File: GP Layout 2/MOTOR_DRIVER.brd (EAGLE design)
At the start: 91.4 x 97.5 mm, 52 parts, among them U3 MIC4604YM, U6 MIC4604YM, U7 ATMEGA328P_TQFP, Y1 16MHz

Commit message: checking that its updated
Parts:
- renumbered BOT_REVERSE to BOT_REV, TOP_REVERSE to TOP_REV, U3 to GATE1, U6 to GATE2
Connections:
- net BLT_RX: now also U$1.8; no longer U$1.7
- net BLT_TX: now also U$1.7; no longer U$1.8
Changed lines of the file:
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@@
 <attribute name="VENDOR" value="TEXAS INSTRUMENTS" x="10.668" y="87.63" size="1.778" layer="27" rot="R90" display="off"/>
 </element>
-<element name="BOT_REVERSE" library="CSD18502KCS" package="KCS3" value="CSD18502KCS_KCS_3" x="16.764" y="87.63" rot="R90">
+<element name="BOT_REV" library="CSD18502KCS" package="KCS3" value="CSD18502KCS_KCS_3" x="16.764" y="87.63" rot="R90">
 <attribute name="MANUFACTURER_PART_NUMBER" value="csd18502kcs_kcs_3" x="16.764" y="87.63" size="1.778" layer="27" rot="R90" display="off"/>
 <attribute name="VENDOR" value="TEXAS INSTRUMENTS" x="16.764" y="87.63" size="1.778" layer="27" rot="R90" display="off"/>
 </element>
-<element name="U3" library="MIC4604" package="SOIC-8_M" value="MIC4604YM" x="17.78" y="74.93" rot="MR270">
+<element name="GATE1" library="MIC4604" package="SOIC-8_M" value="MIC4604YM" x="17.78" y="74.93" rot="MR270">
 <attribute name="MANUFACTURER_PART_NUMBER" value="mic4604ym" x="17.78" y="74.93" size="1.778" layer="28" rot="MR270" display="off"/>
 <attribute name="VENDOR" value="Microchip" x="17.78" y="74.93" size="1.778" layer="28" rot="MR270" display="off"/>
 </element>
-<element name="TOP_REVERSE" library="CSD18502KCS" package="KCS3" value="CSD18502KCS_KCS_3" x="16.51" y="60.96" rot="R270">
+<element name="TOP_REV" library="CSD18502KCS" package="KCS3" value="CSD18502KCS_KCS_3" x="16.51" y="60.96" rot="R270">
 <attribute name="MANUFACTURER_PART_NUMBER" value="csd18502kcs_kcs_3" x="16.51" y="60.96" size="1.778" layer="27" rot="R270" display="off"/>
 <attribute name="VENDOR" value="TEXAS INSTRUMENTS" x="16.51" y="60.96" size="1.778" layer="27" rot="R270" display="off"/>
@@
 <attribute name="VENDOR" value="TEXAS INSTRUMENTS" x="10.16" y="60.96" size="1.778" layer="27" rot="R270" display="off"/>
 </element>
-<element name="U6" library="MIC4604" package="SOIC-8_M" value="MIC4604YM" x="30.48" y="74.93" rot="MR270">
+<element name="GATE2" library="MIC4604" package="SOIC-8_M" value="MIC4604YM" x="30.48" y="74.93" rot="MR270">
 <attribute name="MANUFACTURER_PART_NUMBER" value="mic4604ym" x="30.48" y="74.93" size="1.778" layer="28" rot="MR270" display="off"/>
 <attribute name="VENDOR" value="Microchip" x="30.48" y="74.93" size="1.778" layer="28" rot="MR270" display="off"/>
@@
 </signal>
 <signal name="N$2">
-<contactref element="U3" pad="8"/>
-<contactref element="BOT_REVERSE" pad="1"/>
+<contactref element="GATE1" pad="8"/>
+<contactref element="BOT_REV" pad="1"/>
 <wire x1="15.875" y1="72.2757" x2="16.764" y2="82.55" width="0" layer="19" extent="16-16"/>
 </signal>
 <signal name="N$3">
 <contactref element="TOP_FWD" pad="1"/>
-<contactref element="U3" pad="3"/>
+<contactref element="GATE1" pad="3"/>
 <wire x1="10.668" y1="82.55" x2="18.415" y2="77.5843" width="0" layer="19" extent="16-16"/>
 </signal>
 <signal name="N$4">
-<contactref element="U3" pad="4"/>
+<contactref element="GATE1" pad="4"/>
 <contactref element="C2" pad="1"/>
 <contactref element="C1" pad="1"/>
@@
 </signal>
 <signal name="N$5">
-<contactref element="U3" pad="2"/>
+<contactref element="GATE1" pad="2"/>
 <contactref element="C2" pad="2"/>
 <contactref element="C1" pad="2"/>
@@
 </signal>
 <signal name="N$9">
-<contactref element="U6" pad="8"/>
+<contactref element="GATE2" pad="8"/>
 <contactref element="BOT_FWD" pad="1"/>
 <wire x1="10.16" y1="66.04" x2="28.575" y2="72.2757" width="0" layer="19" extent="16-16"/>
 </signal>
 <signal name="N$10">
-<contactref element="TOP_REVERSE" pad="1"/>
-<contactref element="U6" pad="3"/>
+<contactref element="TOP_REV" pad="1"/>
+<contactref element="GATE2" pad="3"/>
 <wire x1="16.51" y1="66.04" x2="31.115" y2="77.5843" width="0" layer="19" extent="16-16"/>
 </signal>
 <signal name="N$11">
-<contactref element="U6" pad="4"/>
+<contactref element="GATE2" pad="4"/>
 <contactref element="C4" pad="1"/>
 <contactref element="C3" pad="1"/>
@@
 </signal>
 <signal name="N$12">
-<contactref element="U6" pad="2"/>
+<contactref element="GATE2" pad="2"/>
 <contactref element="C4" pad="2"/>
 <contactref element="C3" pad="2"/>
@@
 </signal>
 <signal name="BLT_RX">
+<contactref element="BLUETOOTH" pad="1"/>
+<contactref element="U$1" pad="8"/>
+<wire x1="27.624" y1="9.598" x2="52.07" y2="35.666" width="0" layer="19" extent="1-1"/>
+</signal>
+<signal name="BLT_TX">
+<contactref element="BLUETOOTH" pad="2"/>
 <contactref element="U$1" pad="7"/>
-<contactref element="BLUETOOTH" pad="1"/>
-<wire x1="25.084" y1="9.598" x2="52.07" y2="35.666" width="0" layer="19" extent="1-1"/>
-</signal>
-<signal name="BLT_TX">
-<contactref element="U$1" pad="8"/>
-<contactref element="BLUETOOTH" pad="2"/>
-<wire x1="27.624" y1="9.598" x2="54.61" y2="35.666" width="0" layer="19" extent="1-1"/>
+<wire x1="25.084" y1="9.598" x2="54.61" y2="35.666" width="0" layer="19" extent="1-1"/>
 </signal>
 <signal name="N$13">
@@
 <contactref element="D3" pad="A1"/>
 <contactref element="TOP_FWD" pad="2"/>
-<contactref element="U3" pad="1"/>
-<contactref element="TOP_REVERSE" pad="2"/>
-<contactref element="U6" pad="1"/>
+<contactref element="GATE1" pad="1"/>
+<contactref element="TOP_REV" pad="2"/>
+<contactref element="GATE2" pad="1"/>
 <contactref element="BIG_SWITCH" pad="GND"/>
 <wire x1="16.51" y1="63.5" x2="-61.39" y2="82.042" width="0" layer="19" extent="1-1"/>
@@
 <signal name="GND_TOP">
 <contactref element="SV5" pad="10"/>
-<contactref element="BOT_REVERSE" pad="3"/>
-<contactref element="U3" pad="7"/>
+<contactref element="BOT_REV" pad="3"/>
+<contactref element="GATE1" pad="7"/>
 <contactref element="BOT_FWD" pad="3"/>
-<contactref element="U6" pad="7"/>
+<contactref element="GATE2" pad="7"/>
 <contactref element="C12" pad="-"/>
 <contactref element="C15" pad="-"/>
@@
 <signal name="MOTOR_HIGH_TOP">
 <contactref element="TOP_FWD" pad="3"/>
-<contactref element="BOT_REVERSE" pad="2"/>
+<contactref element="BOT_REV" pad="2"/>
 <contactref element="LSP3" pad="MP"/>
 <contactref element="SV6" pad="5"/>
@@
 </signal>
 <signal name="MOTOR_LOW_TOP">
-<contactref element="TOP_REVERSE" pad="3"/>
+<contactref element="TOP_REV" pad="3"/>
 <contactref element="BOT_FWD" pad="2"/>
 <contactref element="LSP6" pad="MP"/>
@@
 <signal name="LI1_TOP">
 <contactref element="SV6" pad="2"/>
-<contactref element="U3" pad="6"/>
+<contactref element="GATE1" pad="6"/>
 <wire x1="15.7" y1="54.98" x2="18.415" y2="72.2757" width="0" layer="19" extent="16-16"/>
 </signal>
 <signal name="HI1_TOP">
 <contactref element="SV6" pad="1"/>
-<contactref element="U3" pad="5"/>
+<contactref element="GATE1" pad="5"/>
 <wire x1="13.16" y1="54.98" x2="19.685" y2="72.2757" width="0" layer="19" extent="16-16"/>
 </signal>
@@
 <signal name="HI2_TOP">
 <contactref element="SV6" pad="3"/>
-<contactref element="U6" pad="6"/>
+<contactref element="GATE2" pad="6"/>
 <wire x1="18.24" y1="54.98" x2="31.115" y2="72.2757" width="0" layer="19" extent="16-16"/>
 </signal>
 <signal name="LI2_TOP">
 <contactref element="SV6" pad="4"/>
-<contactref element="U6" pad="5"/>
+<contactref element="GATE2" pad="5"/>
 <wire x1="20.78" y1="54.98" x2="32.385" y2="72.2757" width="0" layer="19" extent="16-16"/>
 </signal>

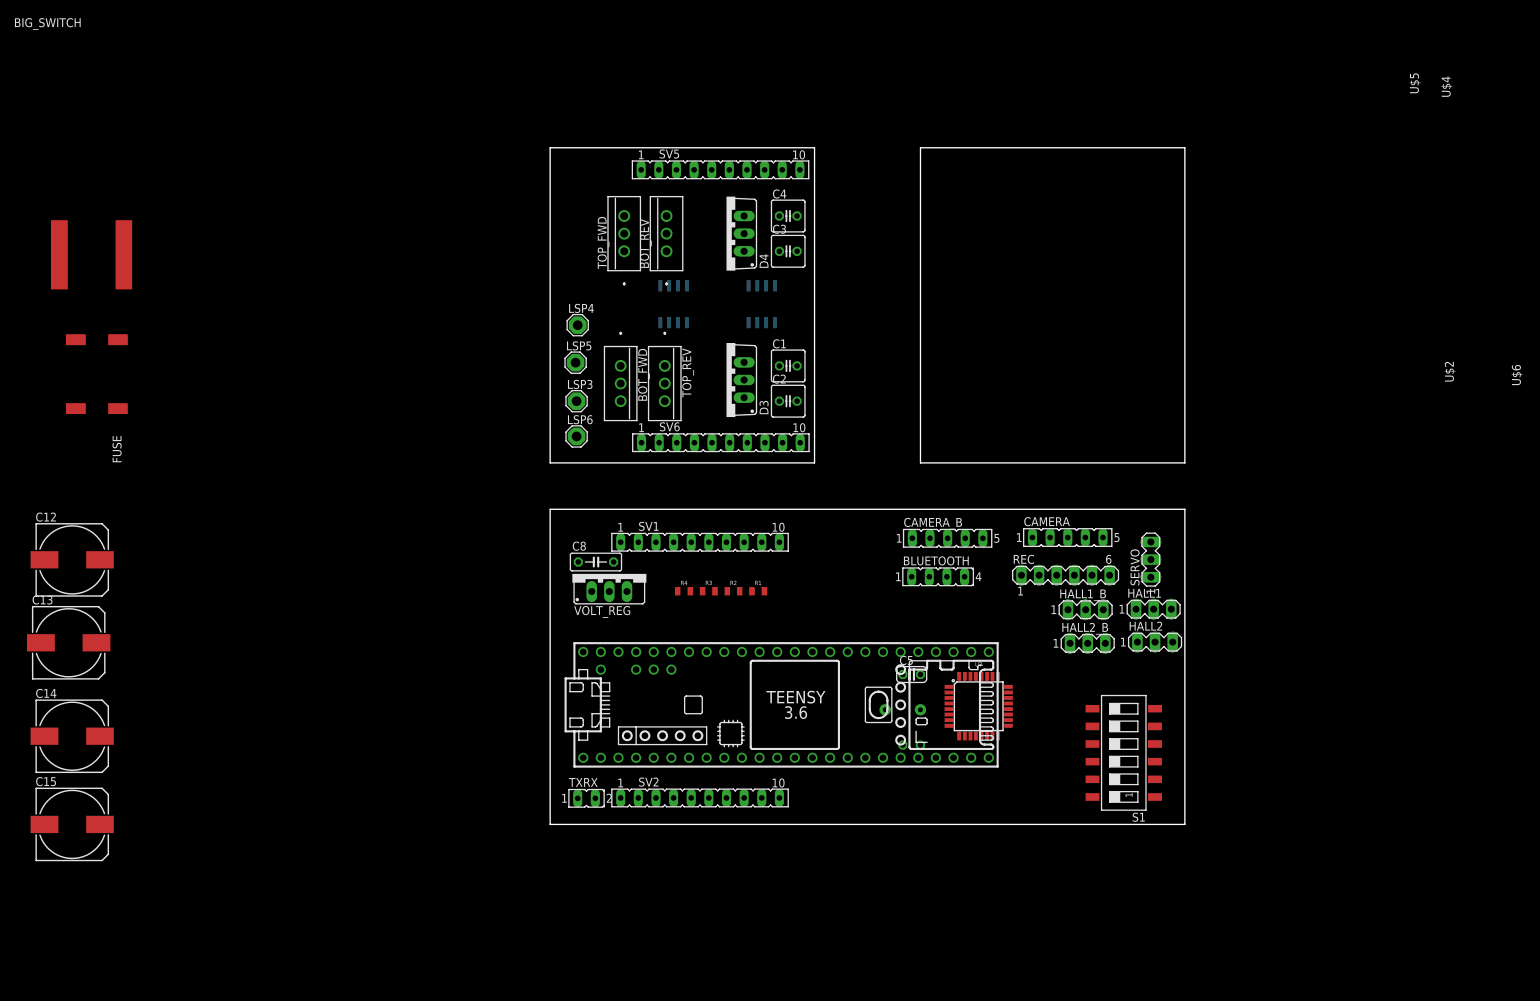
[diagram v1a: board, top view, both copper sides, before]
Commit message: added gpio, modified layout
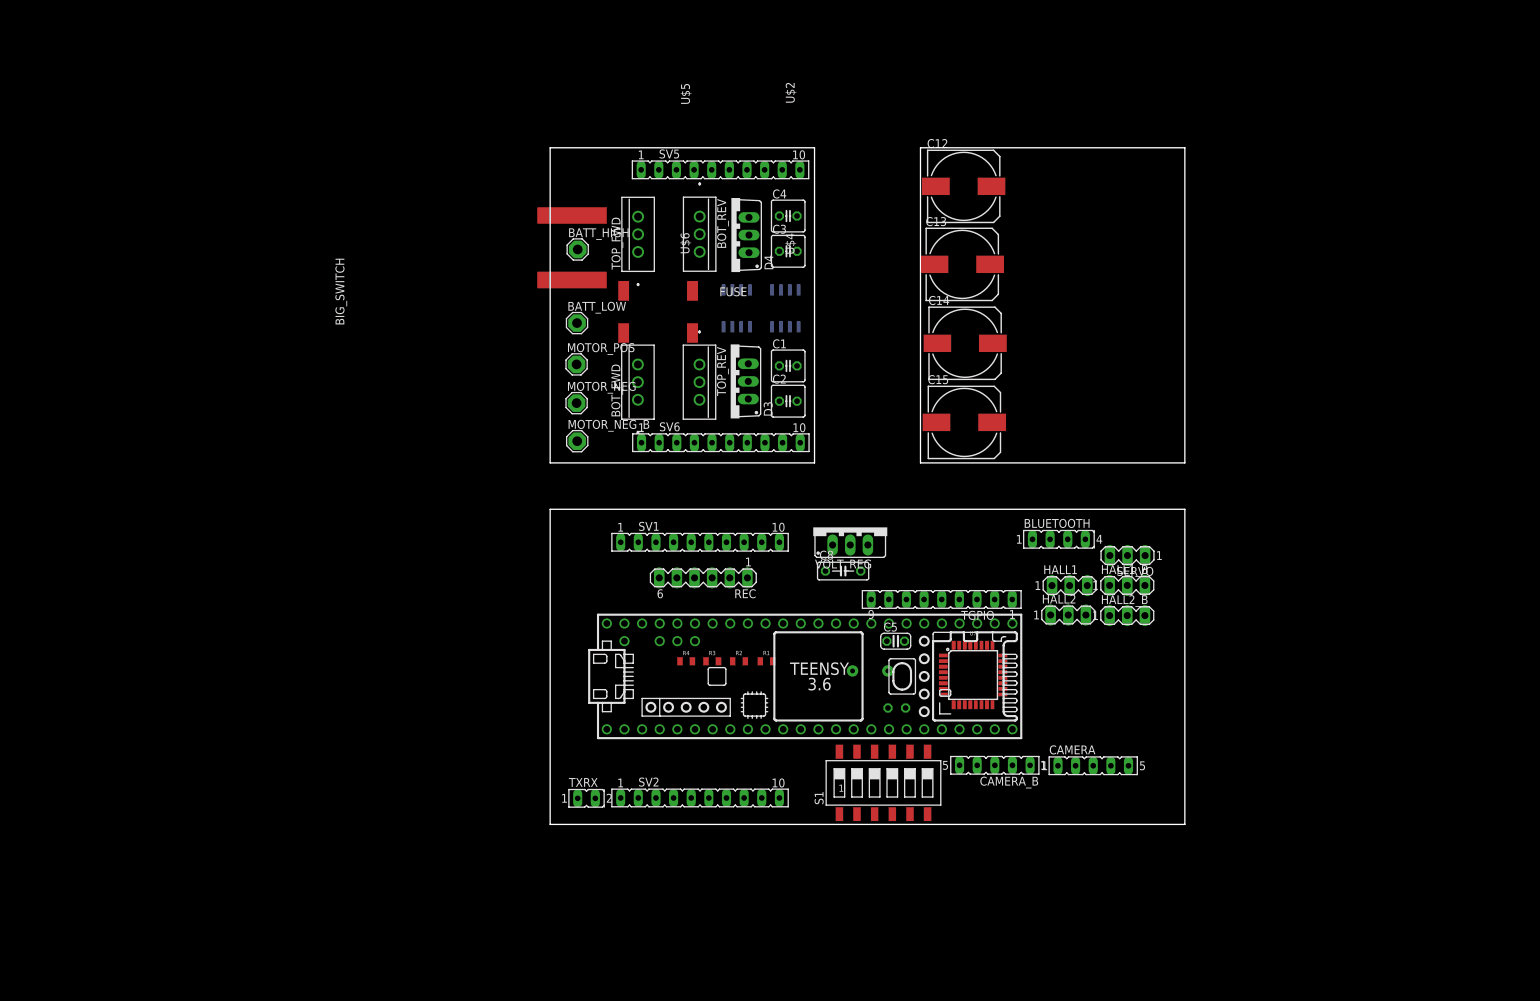
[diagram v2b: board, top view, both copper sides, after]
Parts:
- removed LSP3, LSP4, LSP5, LSP6: SE14, solpad:SE14
- added BATT_HIGH, BATT_LOW, MOTOR_NEG, MOTOR_NEG_B, MOTOR_POS: SE14, solpad:SE14
- added TGPIO: (no value), con-lsta:FE09
- moved U$6 142.2 mm to (8.99, 63.6), turned to 270 degrees
- moved C15 140.9 mm to (59.7, 57.9)
- moved C14 140.5 mm to (59.8, 69.3)
- moved C13 139.8 mm to (59.4, 80.7)
- moved C12 139.2 mm to (59.6, 91.9)
- moved U$2 115.8 mm to (24.1, 85.3), turned to 270 degrees
- moved U$5 105.0 mm to (9.05, 85.1)
- moved U$4 97.2 mm to (24.1, 63.5)
- moved FUSE 81.3 mm to (15.5, 73.8), turned to 0 degrees
- moved BIG_SWITCH 69.2 mm to (3.16, 83.1), turned to 90 degrees
- moved REC 52.2 mm to (22.1, 35.5), turned to 180 degrees
- moved C8 35.6 mm to (42.2, 36.5)
- moved VOLT_REG 35.3 mm to (43.2, 42.8)
- moved S1 34.9 mm to (48.0, 5.98), turned to 0 degrees
- moved CAMERA_B 33.4 mm to (64.0, 8.51), turned to 180 degrees
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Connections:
- removed net M1_GPIO4: U7.1
- new net LED1: U$1.14/A0
- new net LED2: U$1.15/A1
- new net LED3: U$1.16/A2
- new net TGPIO1: TGPIO.1, U$1.33/A14
- new net TGPIO2: TGPIO.2, U$1.34/A15
- new net TGPIO3: TGPIO.3, U$1.35/A16
- new net TGPIO4: TGPIO.4, U$1.36/A17
- new net TGPIO5: TGPIO.5, U$1.37/A18
- new net TGPIO6: TGPIO.6, U$1.38/A19
- new net TGPIO7: TGPIO.7, U$1.39/A20
- new net TGPIO8: TGPIO.8, U$1.21/DAC0
- new net TGPIO9: TGPIO.9, U$1.A22/DAC1
- net BATT_VOLTAGE: now also BATT_HIGH.MP; no longer LSP4.MP
- net BATT_VOLTAGE_SENSE: now also U$1.17/A3; no longer U$1.14/A0
- net EMF_SENSE_HIGH: now also U$1.19/A5/SCL; no longer U$1.17/A3
- net EMF_SENSE_LOW: now also U$1.18/A4/SDA; no longer U$1.16/A2
- net GND_TOP: now also BATT_LOW.MP, MOTOR_NEG_B.MP; no longer LSP5.MP
- net HALL1_B: now also U$1.1/TX; no longer U$1.39/A20
- net HALL2: now also U7.1
- net HALL2_B: now also U$1.2; no longer U$1.38/A19
- net MOTOR_HIGH_TOP: now also MOTOR_POS.MP; no longer LSP3.MP
- net MOTOR_LOW_TOP: now also MOTOR_NEG.MP; no longer LSP6.MP
- net REC_EXTRA1: now also U$1.22/A8
- net REC_EXTRA2: now also U$1.23/A9
- net REC_MOTOR: now also REC.4, U$1.21/A7; no longer REC.3, U$1.15/A1
- net REC_SERVO: now also REC.3, U$1.20/A6; no longer REC.4, U$1.18/A4/SDA
- net SERVO: now also U$1.9/CS; no longer U$1.20/A6
